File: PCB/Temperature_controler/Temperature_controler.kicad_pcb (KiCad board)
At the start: 4 copper layers, 100 x 80 mm, 110 parts, among them J1 RTD1 IN, J10 24V IN, J11 Conn_01x02_Socket, J12 Conn_01x02_Socket, J13 Conn_01x02_Socket, J15 Conn_01x02_Socket, J2 T1 IN, J3 Conn_02x03, J4 T2 IN, J5 RTD2 IN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

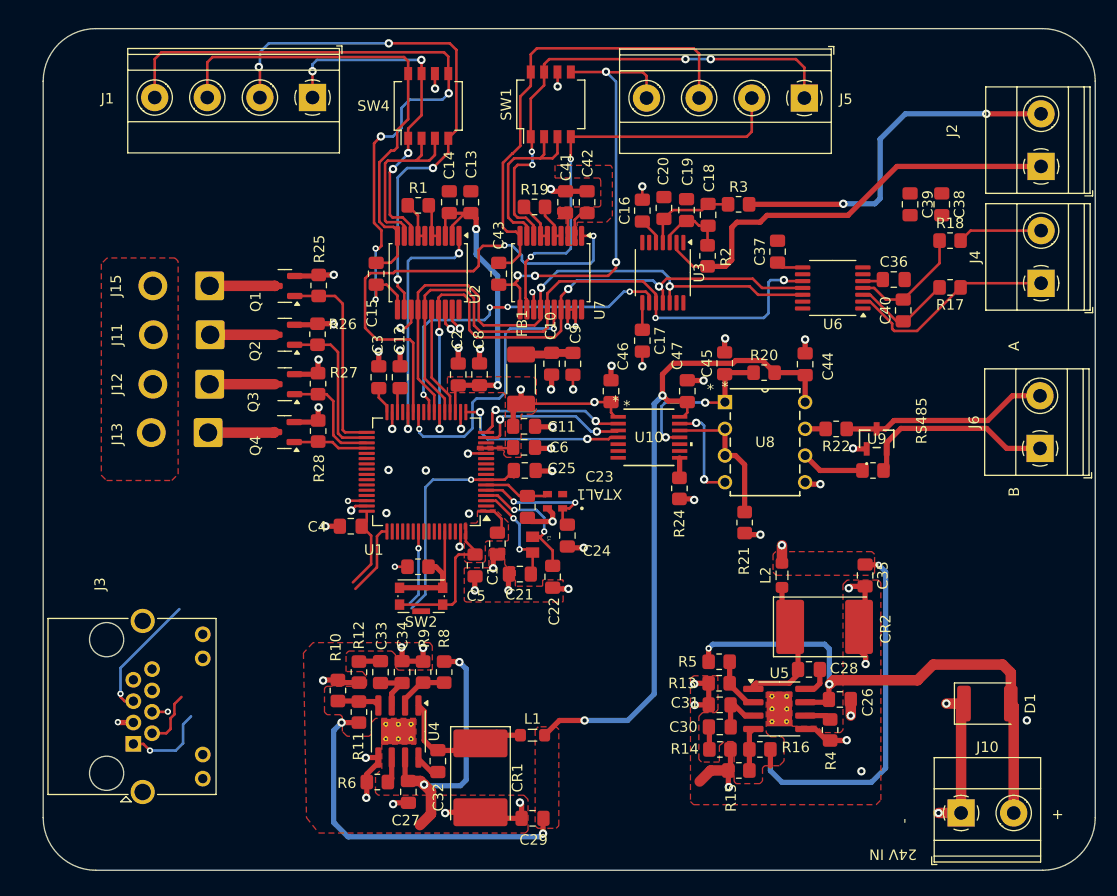
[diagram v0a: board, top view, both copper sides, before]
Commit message: PCB layout progress and PDF for review added
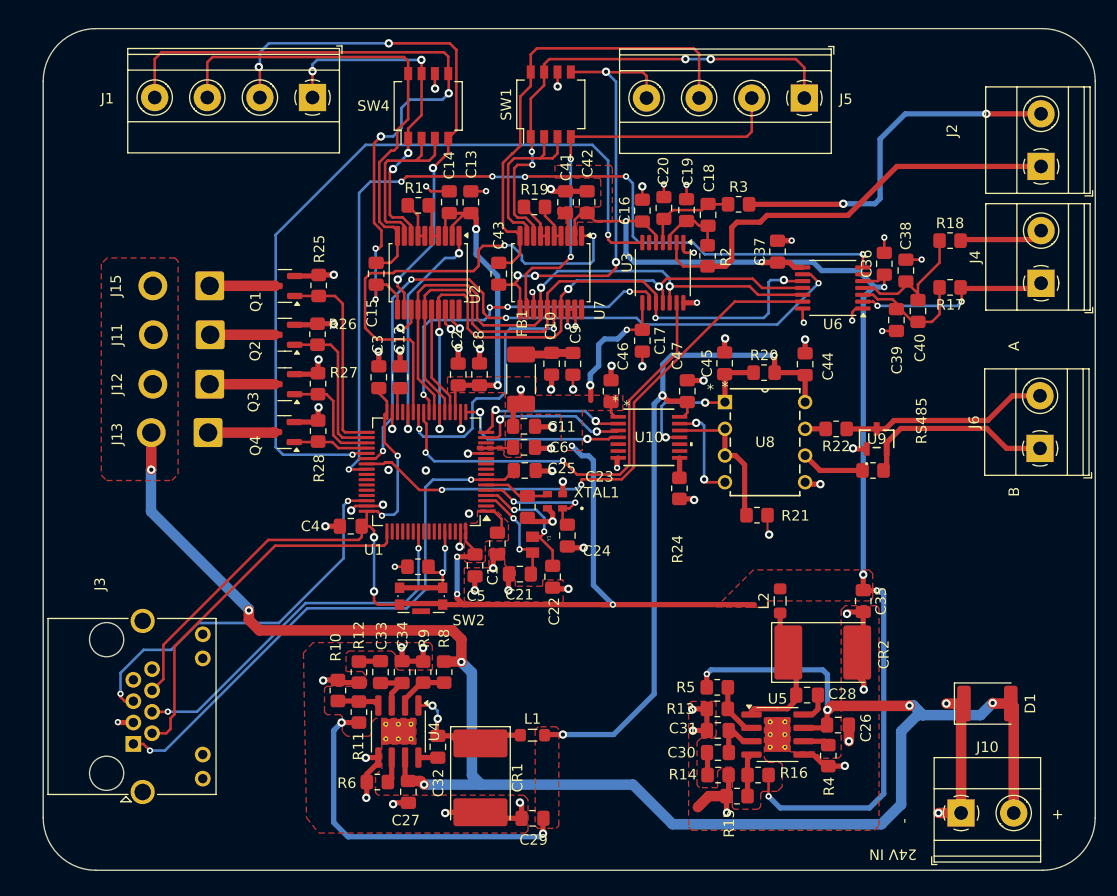
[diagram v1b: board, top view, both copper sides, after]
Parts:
- moved C39 11.1 mm to (141.1, 67.7), turned to 90 degrees
- moved C38 7.16 mm to (142.0, 63.0), turned to 90 degrees
- moved CR2 2.44 mm to (134.1, 99.3)
- moved C30 2.44 mm to (124.1, 108.8)
- moved C31 2.44 mm to (124.1, 106.7)
- moved R14 2.44 mm to (124.2, 111.0)
- moved R15 2.44 mm to (126.0, 113.0)
- moved R16 2.44 mm to (128.0, 111.0)
- moved R5 2.44 mm to (124.1, 102.6)
- moved C26 2.44 mm to (135.6, 106.2)
- moved L2 2.44 mm to (130.1, 94.4)
- moved C35 2.44 mm to (137.9, 94.4)
- moved R4 2.44 mm to (134.6, 109.1)
- moved R13 2.44 mm to (124.1, 104.7)
- moved C28 2.44 mm to (132.6, 103.3)
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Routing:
- net +3.3V: track 129.8 -> 289.8 mm, vias 6 -> 19
- net +24V: track 77.8 -> 172.9 mm, vias 4 -> 8
- net TC2_DRDY: track 0.00 -> 84.2 mm, vias 0 -> 6
- net TC1_DRDY: track 0.00 -> 75.8 mm, vias 0 -> 2
- net TC2_CS: track 0.00 -> 64.3 mm, vias 0 -> 4
- net TC2_FAULT: track 0.00 -> 54.3 mm, vias 0 -> 2
- net TC1_FAULT: track 0.00 -> 42.0 mm, vias 0 -> 2
- net SWO: track 8.71 -> 35.6 mm
- net NRST: track 29.9 -> 53.8 mm
- net SWDIO: track 13.9 -> 36.8 mm
- net SWCLK: track 12.4 -> 35.3 mm
- net GND: track 150.1 -> 172.9 mm, vias 69 -> 81
- net Net-(U6-T+): track 11.3 -> 14.8 mm
- net +5V: track 98.0 -> 99.9 mm, vias 4 -> 5
- net RTD1_DRDY: track 24.4 -> 22.5 mm
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
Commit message: Schematic update, PCB progress
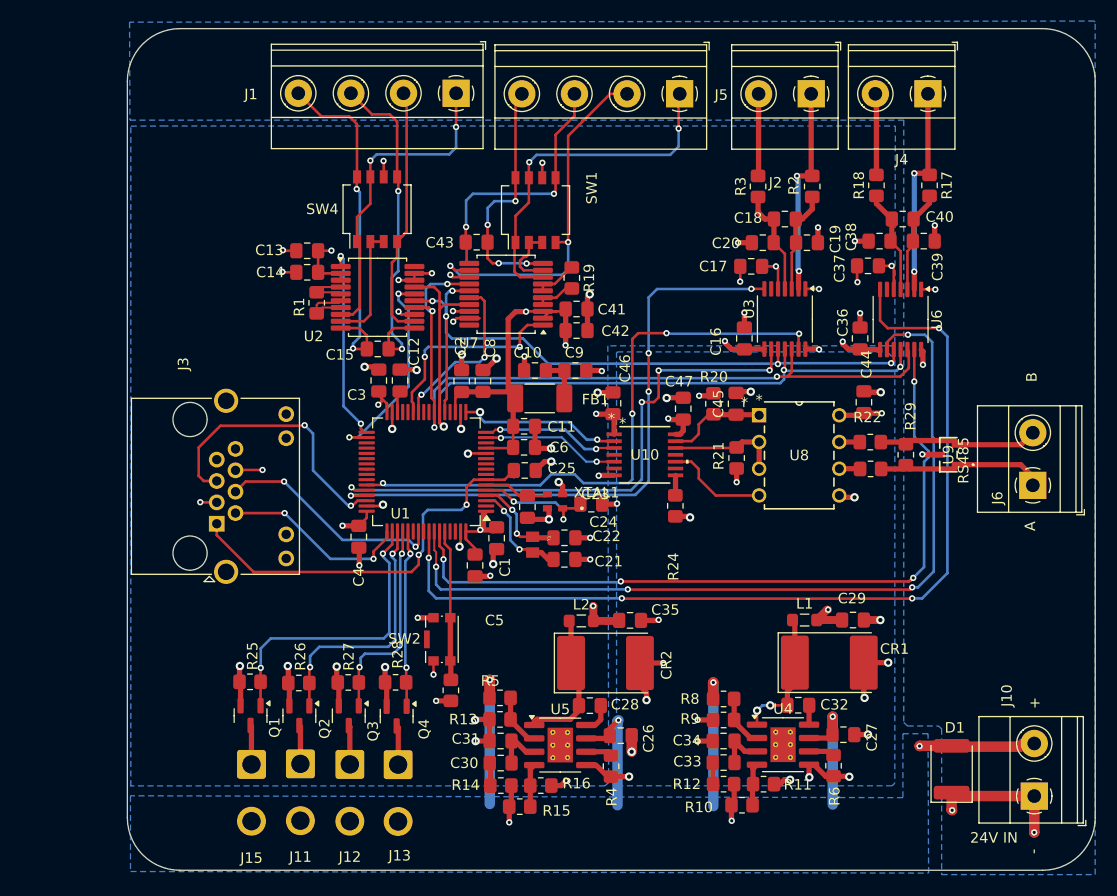
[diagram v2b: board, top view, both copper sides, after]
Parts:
- added R29: 10Ω, Resistor_SMD:R_0805_2012Metric_Pad1.20x1.40mm_HandSolder, F.Cu at (142.0, 80.5)
- moved J15 45.7 mm to (79.8, 109.9), turned to -90 degrees
- moved R6 43.4 mm to (135.1, 110.1), turned to -90 degrees
- moved C27 41.7 mm to (136.1, 107.1), turned to 0 degrees
- moved J11 41.7 mm to (84.5, 109.9), turned to -90 degrees
- moved Q1 41.0 mm to (79.7, 105.3), turned to -90 degrees
- moved R10 39.9 mm to (126.4, 113.8), turned to 0 degrees
- moved R11 39.1 mm to (128.5, 111.8), turned to 180 degrees
- moved J12 38.5 mm to (89.2, 109.9), turned to -90 degrees
- moved R25 38.2 mm to (79.7, 102.1), turned to 180 degrees
- moved U4 36.6 mm to (130.3, 108.1), turned to 0 degrees
- moved J13 36.4 mm to (93.7, 110.0), turned to -90 degrees
- moved R12 36.3 mm to (124.7, 111.8), turned to 0 degrees
- moved Q2 36.2 mm to (84.3, 105.3), turned to -90 degrees
- moved C29 35.8 mm to (137.0, 96.2), turned to 0 degrees
- moved CR1 34.9 mm to (134.7, 100.3), turned to 0 degrees
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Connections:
- C45 pad 1: Net-(U10-B3) -> Net-(U10-B1)
- J1 pad 3: RTD1_RTDIN+ -> RTD1_RTDIN-
- J1 pad 4: RTD1_RTDIN- -> RTD1_RTDIN+
- J5 pad 3: RTD2_RTDIN+ -> RTD2_RTDIN-
- J5 pad 4: RTD2_RTDIN- -> RTD2_RTDIN+
- R20 pad 1: Net-(U10-B3) -> Net-(U10-B1)
- U1 pad 15: RS485_DIR -> RS485_Tx
- U1 pad 16: RS485_Tx -> RS485_DIR
- U1 pad 20: RTD1_CS -> unconnected-(U1-PA4-Pad20)
- U1 pad 24: TC1_CS -> unconnected-(U1-PC4-Pad24)
- U1 pad 25: TC1_FAULT -> unconnected-(U1-PC5-Pad25)
- U1 pad 28: RTD1_DRDY -> unconnected-(U1-PB2-Pad28)
- U1 pad 33: SSR1 -> RTD1_DRDY
- U1 pad 34: SSR2 -> RTD1_CS
- U1 pad 35: SSR3 -> unconnected-(U1-PB14-Pad35)
- U1 pad 36: SSR4 -> unconnected-(U1-PB15-Pad36)
- U1 pad 37: TC1_DRDY -> unconnected-(U1-PC6-Pad37)
- U1 pad 38: TC2_CS -> unconnected-(U1-PC7-Pad38)
- U1 pad 39: TC2_FAULT -> unconnected-(U1-PC8-Pad39)
- U1 pad 40: TC2_DRDY -> unconnected-(U1-PC9-Pad40)
- U1 pad 43: unconnected-(U1-PA10-Pad43) -> TC1_FAULT
- U1 pad 44: unconnected-(U1-PA11-Pad44) -> TC1_CS
- U1 pad 45: unconnected-(U1-PA12-Pad45) -> TC1_DRDY
- U1 pad 50: unconnected-(U1-PA15-Pad50) -> SSR1
- U1 pad 51: unconnected-(U1-PC10-Pad51) -> SSR2
- U1 pad 52: unconnected-(U1-PC11-Pad52) -> SSR3
- U1 pad 53: unconnected-(U1-PC12-Pad53) -> SSR4
- U1 pad 57: unconnected-(U1-PB5-Pad57) -> TC2_DRDY
- U1 pad 58: unconnected-(U1-PB6-Pad58) -> TC2_CS
- U1 pad 59: unconnected-(U1-PB7-Pad59) -> TC2_FAULT
- U10 pad 10: unconnected-(U10-B4-Pad10) -> Net-(U10-B4)
- U10 pad 11: Net-(U10-B3) -> unconnected-(U10-B3-Pad11)
- U10 pad 2: RS485_Tx -> RS485_RX
- U10 pad 4: RS485_RX -> unconnected-(U10-A3-Pad4)
- U10 pad 5: unconnected-(U10-A4-Pad5) -> RS485_Tx
- U8 pad 1: Net-(U10-B3) -> Net-(U10-B1)
- U8 pad 4: Net-(U10-B1) -> Net-(U10-B4)
- U9 pad 1: GND -> Net-(J6-Pin_1)
- U9 pad 2: Net-(J6-Pin_1) -> Net-(J6-Pin_2)
- U9 pad 3: Net-(J6-Pin_2) -> GND
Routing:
- net +3.3V: track 289.8 -> 86.1 mm, vias 19 -> 16
- net +24V: track 172.9 -> 62.6 mm, vias 8 -> 5
- net +5V: track 99.9 -> 15.1 mm
- net RTD1_RTDIN-: track 66.4 -> 33.4 mm, vias 4 -> 2
- net RTD1_FORCE-: track 51.0 -> 24.2 mm, vias 4 -> 0
- net T1+: track 34.6 -> 7.82 mm, vias 2 -> 0
- net RTD2_DRDY: track 44.9 -> 19.4 mm
- net T1-: track 42.3 -> 20.0 mm, vias 0 -> 2
- net TC1_CS: track 32.4 -> 54.0 mm
- net RTD2_RTDIN+: track 44.3 -> 23.6 mm, vias 0 -> 4
- net RTD2_RTDIN-: track 43.4 -> 25.1 mm, vias 4 -> 2
- net TC2_FAULT: track 54.3 -> 72.4 mm, vias 2 -> 4
- net SWCLK: track 35.3 -> 18.6 mm, vias 0 -> 2
- net TC1_DRDY: track 75.8 -> 59.2 mm, vias 2 -> 4
- net TC2_CS: track 64.3 -> 80.8 mm
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- added copper zone on B.Cu, net +24V
- added copper zone on B.Cu, net +3.3V
- added copper zone on B.Cu, net +5V
- added copper zone on B.Cu, net GND
- removed copper zone on F.Cu, net +24V
- removed copper zone on F.Cu, net +3.3V
- removed copper zone on F.Cu, net +5V
- removed copper zone on F.Cu, net GND
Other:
- board size 100 x 80 mm -> 92 x 80 mm

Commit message: PCB traces changed
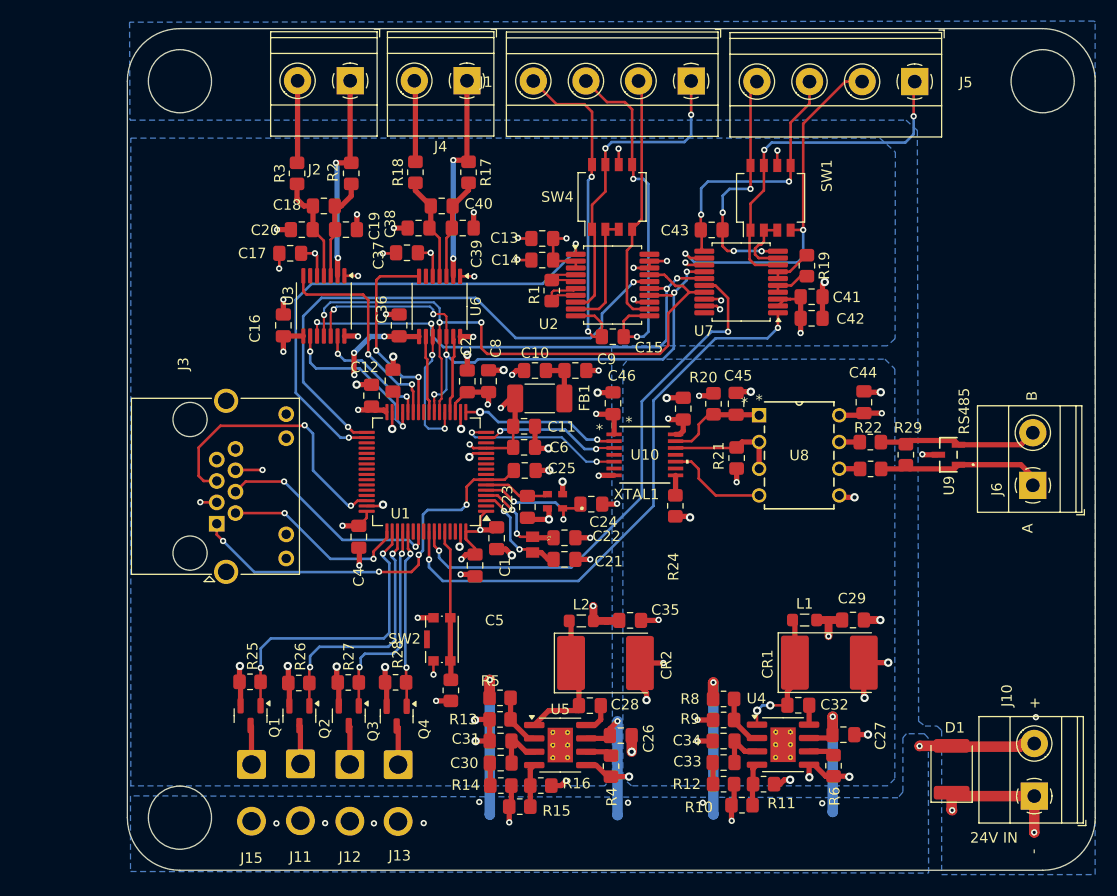
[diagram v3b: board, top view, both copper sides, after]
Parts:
- moved C16 43.8 mm to (82.8, 68.2)
- moved C20 43.8 mm to (84.6, 59.1)
- moved C36 43.8 mm to (93.8, 68.2)
- moved C37 43.8 mm to (94.6, 61.3)
- moved R3 43.8 mm to (84.1, 53.8)
- moved C17 43.8 mm to (83.5, 61.4)
- moved C18 43.8 mm to (86.7, 56.9)
- moved C19 43.8 mm to (88.8, 59.1)
- moved C38 43.8 mm to (95.7, 59.0)
- moved C39 43.8 mm to (99.9, 59.0)
- moved C40 43.8 mm to (97.9, 56.9)
- moved J2 43.8 mm to (89.2, 45.0)
- moved J4 43.8 mm to (100.3, 45.0)
- moved R17 43.8 mm to (100.4, 53.7)
- moved R18 43.8 mm to (95.4, 53.7)
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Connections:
- U1 pad 15: RS485_Tx -> RS485_DIR
- U1 pad 16: RS485_DIR -> RS485_TX
- U1 pad 20: unconnected-(U1-PA4-Pad20) -> TC2_FAULT
- U1 pad 24: unconnected-(U1-PC4-Pad24) -> TC2_CS
- U1 pad 26: RTD2_CS -> TC2_DRDY
- U1 pad 27: RTD2_DRDY -> TC1_DRDY
- U1 pad 28: unconnected-(U1-PB2-Pad28) -> TC1_FAULT
- U1 pad 29: unconnected-(U1-PB10-Pad29) -> TC1_CS
- U1 pad 33: RTD1_DRDY -> RTD1_CS
- U1 pad 34: RTD1_CS -> RTD1_DRDY
- U1 pad 43: TC1_FAULT -> unconnected-(U1-PA10-Pad43)
- U1 pad 44: TC1_CS -> unconnected-(U1-PA11-Pad44)
- U1 pad 45: TC1_DRDY -> unconnected-(U1-PA12-Pad45)
- U1 pad 57: TC2_DRDY -> RTD2_DRDY
- U1 pad 58: TC2_CS -> RTD2_CS
- U1 pad 59: TC2_FAULT -> unconnected-(U1-PB7-Pad59)
- U10 pad 5: RS485_Tx -> RS485_TX
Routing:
- net TC2_CS: track 80.8 -> 7.08 mm, vias 4 -> 0
- net TC2_DRDY: track 88.7 -> 19.3 mm, vias 4 -> 2
- net TC2_FAULT: track 72.4 -> 7.38 mm, vias 4 -> 0
- net TC1_FAULT: track 57.2 -> 11.5 mm, vias 4 -> 2
- net TC1_CS: track 54.0 -> 16.0 mm, vias 4 -> 2
- net TC1_DRDY: track 59.2 -> 21.2 mm, vias 4 -> 2
- net RTD2_DRDY: track 19.4 -> 54.4 mm
- net RTD2_CS: track 16.2 -> 51.1 mm
- net RTD1_CS: track 20.0 -> 52.7 mm
- net RTD1_DRDY: track 18.9 -> 47.6 mm
- net RS485_TX: track 0.00 -> 16.1 mm, vias 0 -> 2
- net SPI1_MOSI: track 74.1 -> 58.5 mm, vias 4 -> 6
- net RS485_Tx: track 13.2 -> 0.00 mm, vias 2 -> 0
- net SPI1_MISO: track 71.0 -> 60.6 mm
- net +3.3V: track 86.1 -> 79.6 mm, vias 16 -> 21
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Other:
- outline, holes or cut-outs redrawn

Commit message: PCB update and sensor abstraction layer
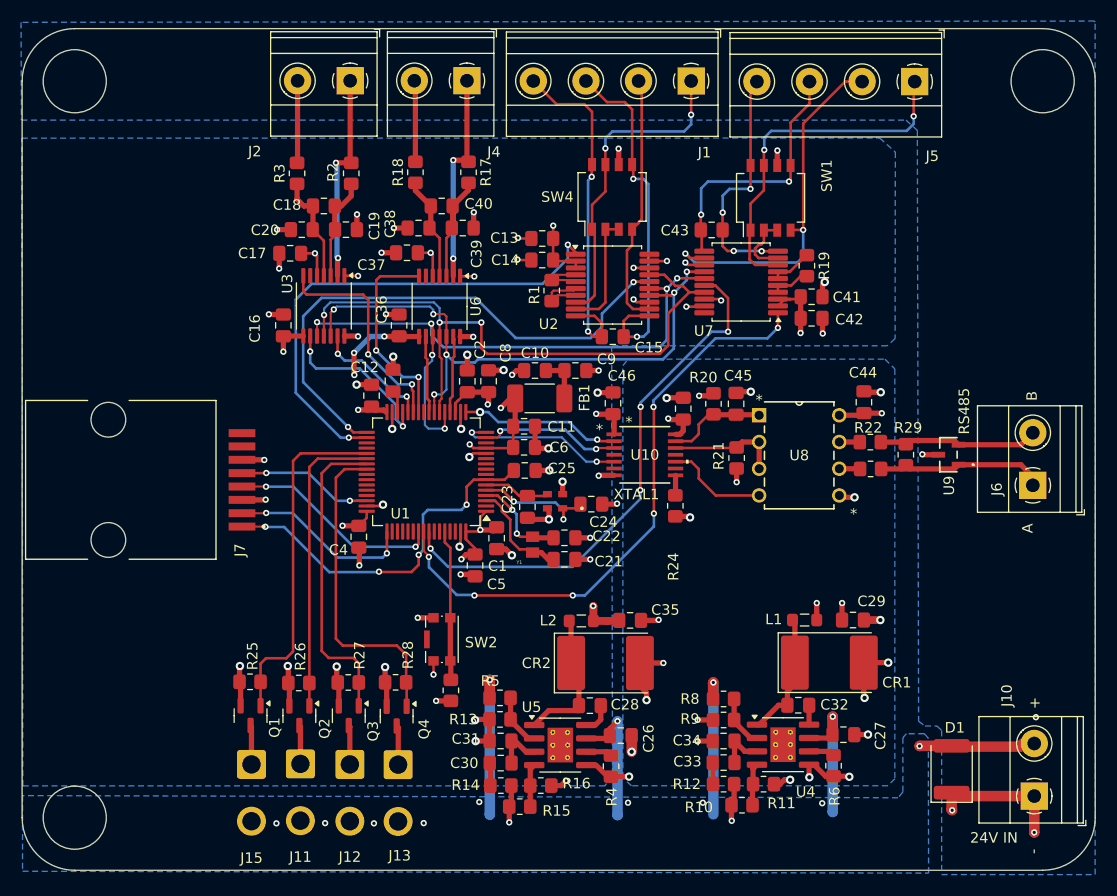
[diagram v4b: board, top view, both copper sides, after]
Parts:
- removed J3: Conn_02x03, Connector_RJ:RJ45_Amphenol_RJHSE538X
- added J7: RJE071880110, RJE071880110:AMPHENOL_RJE071880110, F.Cu at (66.2, 82.9)
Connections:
- U1 pad 37: unconnected-(U1-PC6-Pad37) -> SSR1
- U1 pad 38: unconnected-(U1-PC7-Pad38) -> SSR2
- U1 pad 39: unconnected-(U1-PC8-Pad39) -> SSR3
- U1 pad 40: unconnected-(U1-PC9-Pad40) -> SSR4
- U1 pad 50: SSR1 -> unconnected-(U1-PA15-Pad50)
- U1 pad 51: SSR2 -> unconnected-(U1-PC10-Pad51)
- U1 pad 52: SSR3 -> unconnected-(U1-PC11-Pad52)
- U1 pad 53: SSR4 -> unconnected-(U1-PC12-Pad53)
- U1 pad 56: unconnected-(U1-PB4-Pad56) -> RTD2_DRDY
- U1 pad 57: RTD2_DRDY -> RTD2_CS
- U1 pad 58: RTD2_CS -> unconnected-(U1-PB6-Pad58)
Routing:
- net SWDIO: track 27.0 -> 13.0 mm
- net SSR4: track 17.0 -> 30.8 mm, vias 2 -> 0
- net SSR3: track 19.9 -> 29.6 mm, vias 2 -> 0
- net SSR1: track 28.5 -> 33.0 mm, vias 2 -> 0
- net SSR2: track 24.1 -> 28.5 mm, vias 2 -> 0
- net NRST: track 38.3 -> 35.2 mm
- net RTD2_DRDY: track 54.4 -> 56.9 mm, vias 2 -> 6
- net SWO: track 21.7 -> 20.4 mm
- net Net-(U4-SW): track 12.9 -> 12.2 mm, vias 2 -> 0
- net +5V: track 14.7 -> 14.0 mm, vias 5 -> 6
- net +3.3V: track 79.6 -> 79.1 mm
- net GND: track 156.2 -> 155.8 mm, vias 87 -> 88
- net RTD2_CS: track 51.1 -> 51.3 mm, vias 2 -> 4
- net LSE_IN: vias 2 -> 0
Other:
- board size 92 x 80 mm -> 102 x 80 mm
